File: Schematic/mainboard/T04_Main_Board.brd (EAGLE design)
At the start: 78.2 x 33.3 mm, 24 parts, among them IC1 7805DT, J1 AVR_SPI_PRG_6PTH, U1 ATMEGA328P_PDIP, Y1 16MHZ

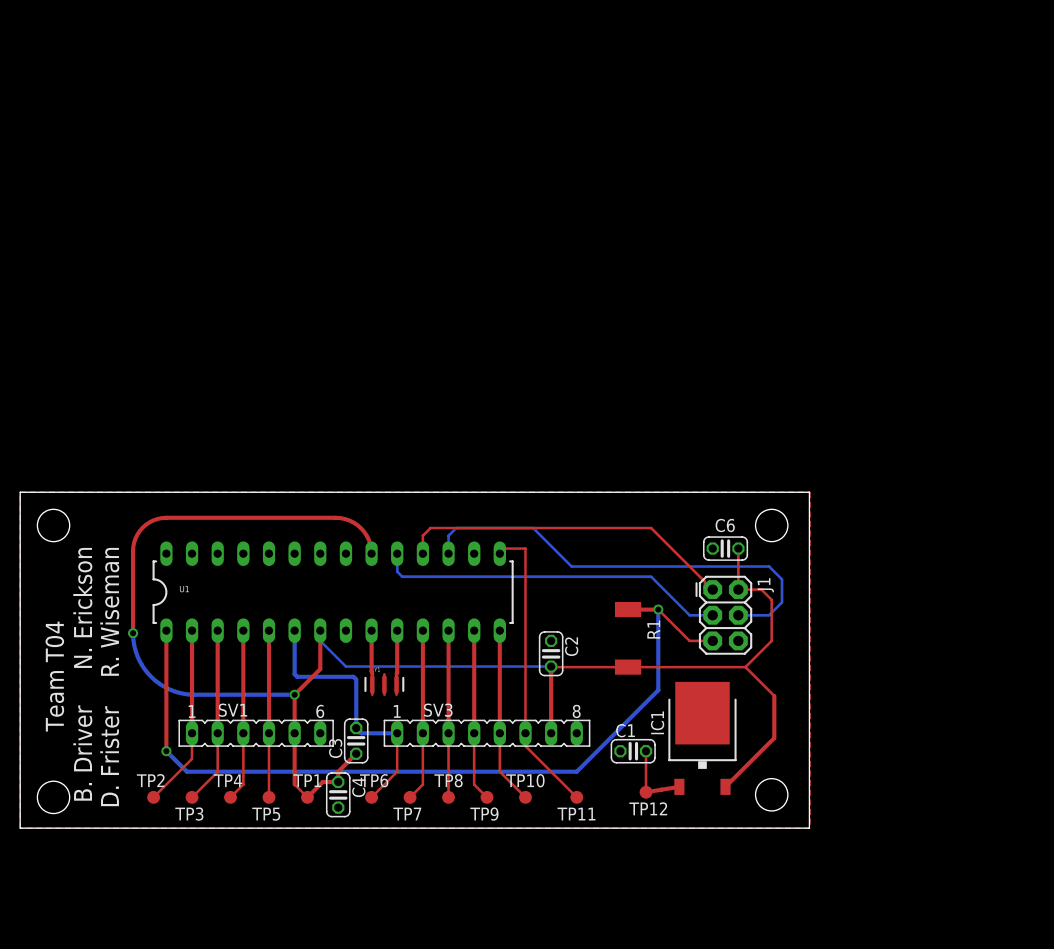
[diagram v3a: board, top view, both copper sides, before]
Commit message: Mainboard layout fixed
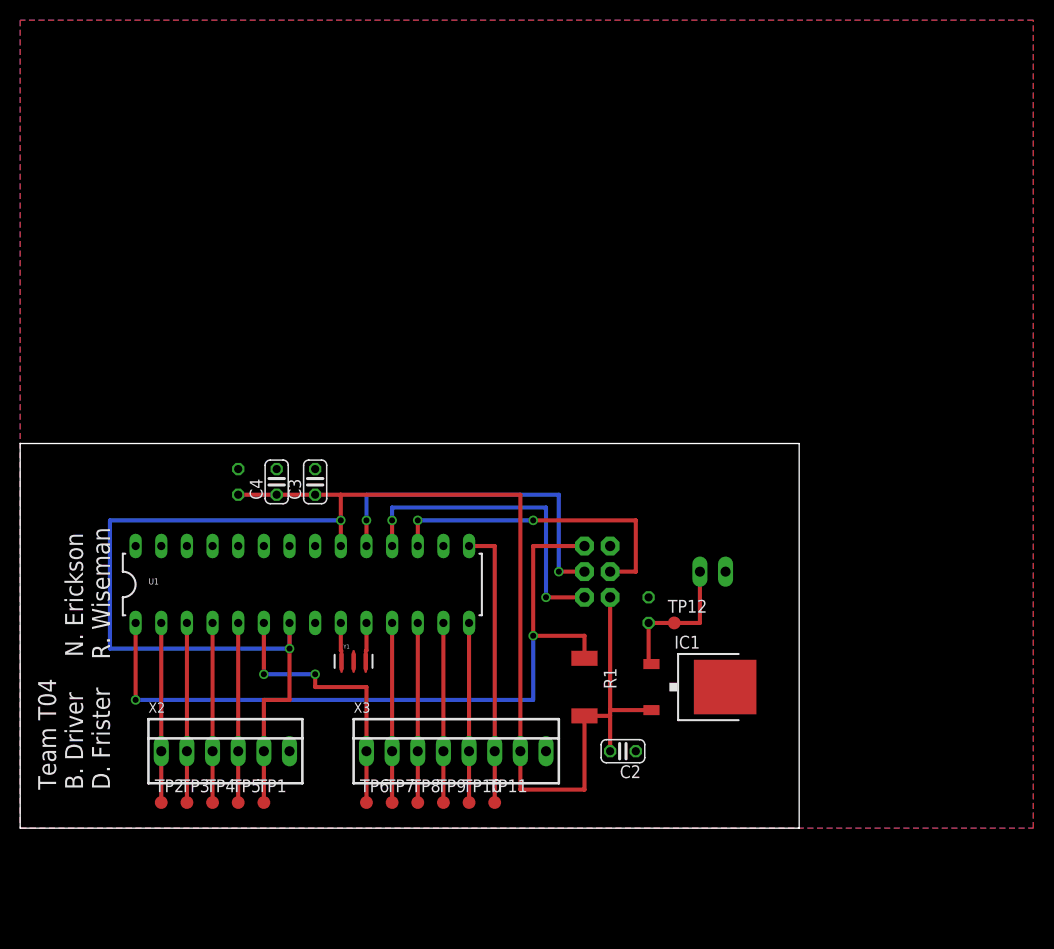
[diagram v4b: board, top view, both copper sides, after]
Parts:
- removed SV1: (no value), con-lsta:FE06
- removed SV3: (no value), con-lsta:FE08
- added X1: 22-23-2021, con-molex:22-23-2021
- added X2: (no value), con-molex:22-23-2061
- added X3: 22-23-2081, con-molex:22-23-2081
- moved C6 48.7 mm to (21.6, 34.3), flipped to the bottom, turned to 90 degrees
- moved C4 31.6 mm to (25.4, 34.3), turned to 90 degrees
- moved C3 26.0 mm to (29.2, 34.3)
- moved TP12 17.0 mm to (64.8, 20.3)
- moved C1 14.1 mm to (62.2, 21.6), flipped to the bottom, turned to 270 degrees
- moved J1 12.7 mm to (55.9, 22.9), flipped to the bottom, turned to 90 degrees
- moved C2 12.0 mm to (59.7, 7.62), turned to 180 degrees
- moved TP11 8.14 mm to (47.0, 2.54)
- moved R1 6.48 mm to (55.9, 14.0)
- moved TP10 5.61 mm to (44.5, 2.54)
- moved IC1 5.09 mm to (67.3, 14.0), turned to 270 degrees
- moved TP9 4.35 mm to (41.9, 2.54)
- moved TP1 4.35 mm to (24.1, 2.54)
- moved Y1 3.81 mm to (33.0, 16.5)
- moved U1 3.14 mm to (27.9, 24.1)
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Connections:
- removed net N$3: Y1.2
- removed net S$1: C1.1, C2.1, C3.2, C4.2, C6.2, IC1.3, J1.6, SV1.6, SV3.1, SV3.8, TP6.TP, U1.22, U1.6, U1.8
- new net GND: C1.1, C2.1, C3.2, C4.2, C6.2, IC1.3, J1.6, U1.22, U1.8, X1.2, X2.6, X3.8, Y1.2
- new net TRIG1: TP6.TP, U1.6, X3.1
- net +12V: now also X1.1
- net +5V: now also X2.5, X3.7; no longer SV1.5, SV3.7
- net BIT0: now also X2.1; no longer SV1.1
- net BIT1: now also X2.2; no longer SV1.2
- net BIT2: now also X2.3; no longer SV1.3
- net BIT3: now also X2.4; no longer SV1.4
- net ECHO1: now also X3.2; no longer SV3.2
- net ECHO2: now also X3.4; no longer SV3.4
- net ECHO3: now also X3.6; no longer SV3.6
- net TRIG2: now also X3.3; no longer SV3.3
- net TRIG3: now also X3.5; no longer SV3.5
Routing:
- net S$1: track 30.7 -> 0.00 mm
- net TRIG1: track 0.00 -> 27.9 mm, vias 0 -> 2
- net +5V: track 160.7 -> 174.0 mm
- net MOSI: track 44.3 -> 31.8 mm, vias 0 -> 2
- net RESET: track 82.5 -> 74.6 mm
- net +12V: track 7.64 -> 14.5 mm
- net MISO: track 33.8 -> 31.8 mm, vias 0 -> 2
- net ECHO3: track 29.5 -> 27.9 mm
- net N$2: track 4.33 -> 2.82 mm
- net N$1: track 4.33 -> 2.82 mm
- net TRIG2: track 16.5 -> 17.8 mm
- net BIT3: track 16.5 -> 17.8 mm
- net ECHO2: track 17.0 -> 17.8 mm
- net ECHO1: track 17.0 -> 17.8 mm
- net BIT2: track 17.0 -> 17.8 mm
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- added copper zone on layer 1, net GND
- added copper zone on layer 16, net GND
- removed copper zone on layer 1, net S$1
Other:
- board size 78.2 x 33.3 mm -> 77.1 x 38.1 mm
- board text added: "Team T04 B. Driver N. Erickson D. Frister R. Wiseman"
- board text removed: "B. Driver N. Erickson D. Frister R. Wiseman"
- board text removed: "Team T04"

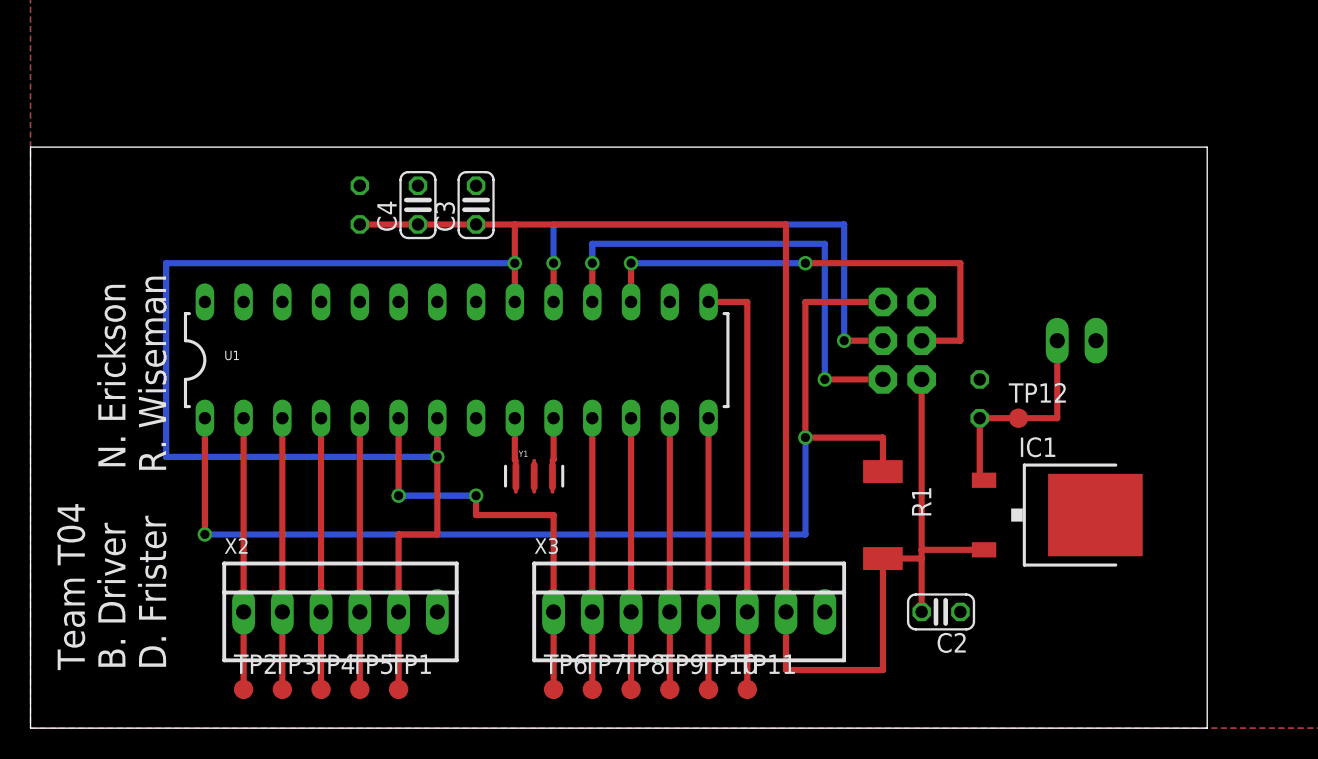
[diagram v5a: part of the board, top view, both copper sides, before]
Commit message: Mainboard & Display layout updates - Molex connectors, Mounting Holes, Greenberg Email Additions
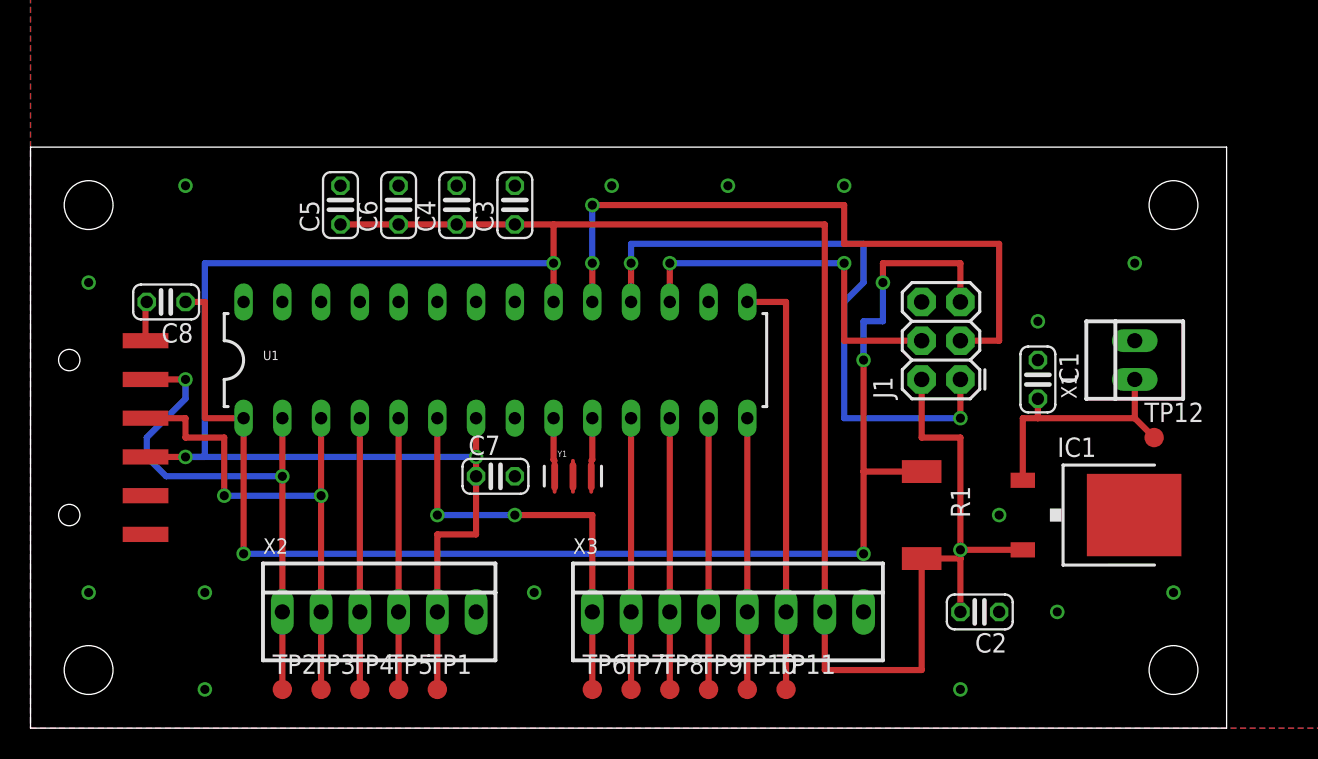
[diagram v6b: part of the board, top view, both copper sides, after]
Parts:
- added C5, C7: 0.1u, rcl:C025-024X044
- added C8: .1u, rcl:C025-024X044
- added JP1: (no value), SparkFun-Connectors:1X06-SMD
- C2: value .1u -> 10uf
- moved TP12 8.98 mm to (73.7, 19.1)
- moved J1 5.08 mm to (61.0, 22.9), flipped to the top
- moved C1 4.02 mm to (66.0, 22.9), flipped to the top
- moved X1 4.02 mm to (72.4, 24.1), flipped to the top, turned to 90 degrees
- moved TP9 2.54 mm to (44.5, 2.54)
- moved C4 2.54 mm to (27.9, 34.3)
- moved TP1 2.54 mm to (26.7, 2.54)
- moved TP2 2.54 mm to (16.5, 2.54)
- moved C2 2.54 mm to (62.2, 7.62)
- moved C3 2.54 mm to (31.8, 34.3)
- moved C6 2.54 mm to (24.1, 34.3), flipped to the top
- moved R1 2.54 mm to (58.4, 14.0)
- moved TP10 2.54 mm to (47.0, 2.54)
- moved TP11 2.54 mm to (49.5, 2.54)
- moved TP3 2.54 mm to (19.1, 2.54)
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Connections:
- new net CTS: JP1.5
- new net DTR: C8.2, JP1.1
- net +5V: now also C5.1, C7.1, JP1.4
- net BIT0: now also JP1.2
- net BIT1: now also JP1.3
- net GND: now also C5.2, C7.2, JP1.6
- net RESET: now also C8.1
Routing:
- net BIT0: track 17.8 -> 35.9 mm, vias 0 -> 2
- net RESET: track 74.6 -> 92.7 mm, vias 2 -> 4
- net BIT1: track 17.8 -> 34.4 mm, vias 0 -> 2
- net SCK: track 34.3 -> 44.4 mm
- net MISO: track 31.8 -> 41.2 mm
- net +5V: track 174.0 -> 182.9 mm, vias 2 -> 4
- net MOSI: track 31.8 -> 24.1 mm
- net +12V: track 14.5 -> 17.3 mm
- net DTR: track 0.00 -> 2.57 mm
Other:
- board size 77.1 x 38.1 mm -> 78.4 x 38.1 mm
- board text added: "T04 Rev 1.0 B. Driver N.Erickson D. Frister R.Wiseman"
- board text removed: "Team T04 B. Driver N. Erickson D. Frister R. Wiseman"

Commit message: M@INb0@RD C0MPl37e
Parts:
- X2: value (none) -> 22-23-2071; device con-molex:22-23-2061 -> con-molex:22-23-2071
- moved TP1 2.54 mm to (29.2, 2.54)
- moved X2 1.27 mm to (24.1, 7.62)
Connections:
- new net MUXENABLE: U1.16, X2.5
- net +5V: now also X2.6; no longer X2.5
- net GND: now also X2.7; no longer X2.6
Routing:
- net MUXENABLE: track 0.00 -> 63.5 mm, vias 0 -> 4
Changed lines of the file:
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@@
 <?xml version="1.0" encoding="utf-8"?>
 <!DOCTYPE eagle SYSTEM "eagle.dtd">
-<eagle version="6.3">
+<eagle version="7.1.0">
 <drawing>
 <settings>
@@
 <pass name="Default">
 <param name="RoutingGrid" value="50mil"/>
+<param name="AutoGrid" value="1"/>
+<param name="Efforts" value="0"/>
+<param name="TopRouterVariant" value="1"/>
 <param name="tpViaShape" value="round"/>
 <param name="PrefDir.1" value="|"/>
@@
 </element>
 <element name="R1" library="rcl" package="M2309" value="10k" x="58.42" y="13.97" rot="R270"/>
-<element name="TP1" library="testpad" package="B1,27" value="TPB1,27" x="26.67" y="2.54">
-<attribute name="TP_SIGNAL_NAME" value="" x="26.67" y="2.54" size="1.778" layer="27" display="off"/>
+<element name="TP1" library="testpad" package="B1,27" value="TPB1,27" x="29.21" y="2.54">
+<attribute name="TP_SIGNAL_NAME" value="" x="29.21" y="2.54" size="1.778" layer="27" display="off"/>
 </element>
 <element name="TP10" library="testpad" package="B1,27" value="TPB1,27" x="46.99" y="2.54">
@@
 <attribute name="MF" value="MOLEX" x="72.39" y="24.13" size="1.778" layer="27" rot="R90" display="off"/>
 <attribute name="OC_FARNELL" value="1462926" x="72.39" y="24.13" size="1.778" layer="27" rot="R90" display="off"/>
-</element>
-<element name="X2" library="con-molex" package="22-23-2061" value="" x="22.86" y="7.62">
-<attribute name="OC_NEWARK" value="27C1933" x="22.86" y="7.62" size="1.778" layer="27" display="off"/>
-<attribute name="MPN" value="22-23-2061" x="22.86" y="7.62" size="1.778" layer="27" display="off"/>
-<attribute name="MF" value="MOLEX" x="22.86" y="7.62" size="1.778" layer="27" display="off"/>
-<attribute name="OC_FARNELL" value="1462922" x="22.86" y="7.62" size="1.778" layer="27" display="off"/>
 </element>
 <element name="X3" library="con-molex" package="22-23-2081" value="22-23-2081" x="45.72" y="7.62" smashed="yes">
@@
 <element name="JP1" library="SparkFun-Connectors" package="1X06-SMD" value="" x="2.54" y="19.05" rot="R270"/>
 <element name="C8" library="rcl" package="C025-024X044" value=".1u" x="8.89" y="27.94" rot="R180"/>
+<element name="X2" library="con-molex" package="22-23-2071" value="22-23-2071" x="24.13" y="7.62">
+<attribute name="OC_NEWARK" value="56H0445" x="24.13" y="7.62" size="1.778" layer="27" display="off"/>
+<attribute name="MPN" value="22-23-2071" x="24.13" y="7.62" size="1.778" layer="27" display="off"/>
+<attribute name="MF" value="MOLEX" x="24.13" y="7.62" size="1.778" layer="27" display="off"/>
+<attribute name="OC_FARNELL" value="1654534" x="24.13" y="7.62" size="1.778" layer="27" display="off"/>
+</element>
 </elements>
 <signals>
@@
 <contactref element="C2" pad="1"/>
 <contactref element="X3" pad="8"/>
-<contactref element="X2" pad="6"/>
 <contactref element="Y1" pad="2"/>
 <contactref element="C5" pad="2"/>
@@
 <via x="11.43" y="8.89" extent="1-16" drill="0.6" shape="square"/>
 <via x="11.43" y="2.54" extent="1-16" drill="0.6" shape="square"/>
-<via x="33.02" y="8.89" extent="1-16" drill="0.6" shape="square"/>
 <via x="67.31" y="7.62" extent="1-16" drill="0.6" shape="square"/>
 <via x="74.93" y="8.89" extent="1-16" drill="0.6" shape="square"/>
@@
 <via x="3.81" y="29.21" extent="1-16" drill="0.6" shape="square"/>
 <via x="63.5" y="13.97" extent="1-16" drill="0.6" shape="square"/>
+<contactref element="X2" pad="7"/>
 </signal>
 <signal name="+5V">
@@
 <wire x1="31.75" y1="33.02" x2="27.94" y2="33.02" width="0.4064" layer="1"/>
 <contactref element="X3" pad="7"/>
-<contactref element="X2" pad="5"/>
-<wire x1="26.67" y1="2.54" x2="26.67" y2="7.62" width="0.4064" layer="1"/>
-<wire x1="26.67" y1="7.62" x2="26.67" y2="12.7" width="0.4064" layer="1"/>
 <wire x1="26.67" y1="12.7" x2="29.21" y2="12.7" width="0.4064" layer="1"/>
 <wire x1="52.07" y1="7.62" x2="52.07" y2="3.81" width="0.4064" layer="1"/>
@@
 <via x="29.21" y="17.78" extent="1-16" drill="0.6" shape="square"/>
 <wire x1="29.21" y1="17.78" x2="10.16" y2="17.78" width="0.4064" layer="16"/>
+<contactref element="X2" pad="6"/>
+<wire x1="29.21" y1="7.62" x2="29.21" y2="12.7" width="0.4064" layer="1"/>
+<wire x1="29.21" y1="2.54" x2="29.21" y2="7.62" width="0.4064" layer="1"/>
 </signal>
 <signal name="+12V">
@@
 <contactref element="U1" pad="2"/>
 <contactref element="TP2" pad="TP"/>
-<contactref element="X2" pad="1"/>
-<wire x1="16.51" y1="2.54" x2="16.51" y2="7.62" width="0.4064" layer="1"/>
-<wire x1="16.51" y1="7.62" x2="16.51" y2="16.51" width="0.4064" layer="1"/>
 <contactref element="JP1" pad="2"/>
 <wire x1="16.51" y1="16.51" x2="16.51" y2="20.32" width="0.4064" layer="1"/>
@@
 <wire x1="8.89" y1="16.51" x2="16.51" y2="16.51" width="0.4064" layer="16"/>
 <via x="16.51" y="16.51" extent="1-16" drill="0.6" shape="square"/>
+<contactref element="X2" pad="1"/>
+<wire x1="16.51" y1="7.62" x2="16.51" y2="16.51" width="0.4064" layer="1"/>
+<wire x1="16.51" y1="2.54" x2="16.51" y2="7.62" width="0.4064" layer="1"/>
 </signal>
 <signal name="BIT1">
 <contactref element="U1" pad="3"/>
 <contactref element="TP3" pad="TP"/>
-<contactref element="X2" pad="2"/>
-<wire x1="19.05" y1="2.54" x2="19.05" y2="7.62" width="0.4064" layer="1"/>
 <wire x1="19.05" y1="20.32" x2="19.05" y2="15.24" width="0.4064" layer="1"/>
 <contactref element="JP1" pad="3"/>
-<wire x1="19.05" y1="15.24" x2="19.05" y2="7.62" width="0.4064" layer="1"/>
 <wire x1="7.54" y1="20.32" x2="10.16" y2="20.32" width="0.4064" layer="1"/>
 <wire x1="10.16" y1="20.32" x2="10.16" y2="19.05" width="0.4064" layer="1"/>
@@
 <wire x1="12.7" y1="15.24" x2="19.05" y2="15.24" width="0.4064" layer="16"/>
 <via x="19.05" y="15.24" extent="1-16" drill="0.6" shape="square"/>
+<contactref element="X2" pad="2"/>
+<wire x1="19.05" y1="7.62" x2="19.05" y2="15.24" width="0.4064" layer="1"/>
+<wire x1="19.05" y1="2.54" x2="19.05" y2="7.62" width="0.4064" layer="1"/>
 </signal>
 <signal name="BIT2">
@@
 <contactref element="TP4" pad="TP"/>
 <contactref element="X2" pad="3"/>
+<wire x1="21.59" y1="20.32" x2="21.59" y2="7.62" width="0.4064" layer="1"/>
 <wire x1="21.59" y1="2.54" x2="21.59" y2="7.62" width="0.4064" layer="1"/>
-<wire x1="21.59" y1="7.62" x2="21.59" y2="20.32" width="0.4064" layer="1"/>
 </signal>
 <signal name="BIT3">
@@
 <contactref element="TP5" pad="TP"/>
 <contactref element="X2" pad="4"/>
+<wire x1="24.13" y1="7.62" x2="24.13" y2="20.32" width="0.4064" layer="1"/>
 <wire x1="24.13" y1="2.54" x2="24.13" y2="7.62" width="0.4064" layer="1"/>
-<wire x1="24.13" y1="20.32" x2="24.13" y2="7.62" width="0.4064" layer="1"/>
 </signal>
 <signal name="SCK">
@@
 <wire x1="7.54" y1="27.86" x2="7.62" y2="27.94" width="0.4064" layer="1"/>
 </signal>
+<signal name="MUXENABLE">
+<contactref element="U1" pad="16"/>
+<contactref element="X2" pad="5"/>
+<wire x1="26.67" y1="7.62" x2="26.67" y2="3.81" width="0.4064" layer="1"/>
+<via x="26.67" y="3.81" extent="1-16" drill="0.6" shape="square"/>
+<wire x1="26.67" y1="3.81" x2="34.29" y2="3.81" width="0.4064" layer="16"/>
+<wire x1="34.29" y1="3.81" x2="34.29" y2="10.16" width="0.4064" layer="16"/>
+<via x="34.29" y="10.16" extent="1-16" drill="0.6" shape="square"/>
+<wire x1="34.29" y1="10.16" x2="34.29" y2="12.7" width="0.4064" layer="1"/>
+<via x="34.29" y="12.7" extent="1-16" drill="0.6" shape="square"/>
+<wire x1="34.29" y1="12.7" x2="50.8" y2="12.7" width="0.4064" layer="16"/>
+<wire x1="50.8" y1="12.7" x2="50.8" y2="29.21" width="0.4064" layer="16"/>
+<via x="50.8" y="29.21" extent="1-16" drill="0.6" shape="square"/>
+<wire x1="50.8" y1="29.21" x2="50.8" y2="30.48" width="0.4064" layer="1"/>
+<wire x1="50.8" y1="30.48" x2="44.45" y2="30.48" width="0.4064" layer="1"/>
+<wire x1="44.45" y1="30.48" x2="44.45" y2="27.94" width="0.4064" layer="1"/>
+</signal>
 </signals>
